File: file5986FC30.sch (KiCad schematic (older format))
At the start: 52 parts, among them Q1 Q_NPN_BEC, Q2 Q_NPN_BEC, Q3 Q_NPN_BEC, Q4 Q_NPN_BEC, U12 CM1224, U15 ufl, U16 ufl, U17 ufl, U3 MIC29302, U5 J502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

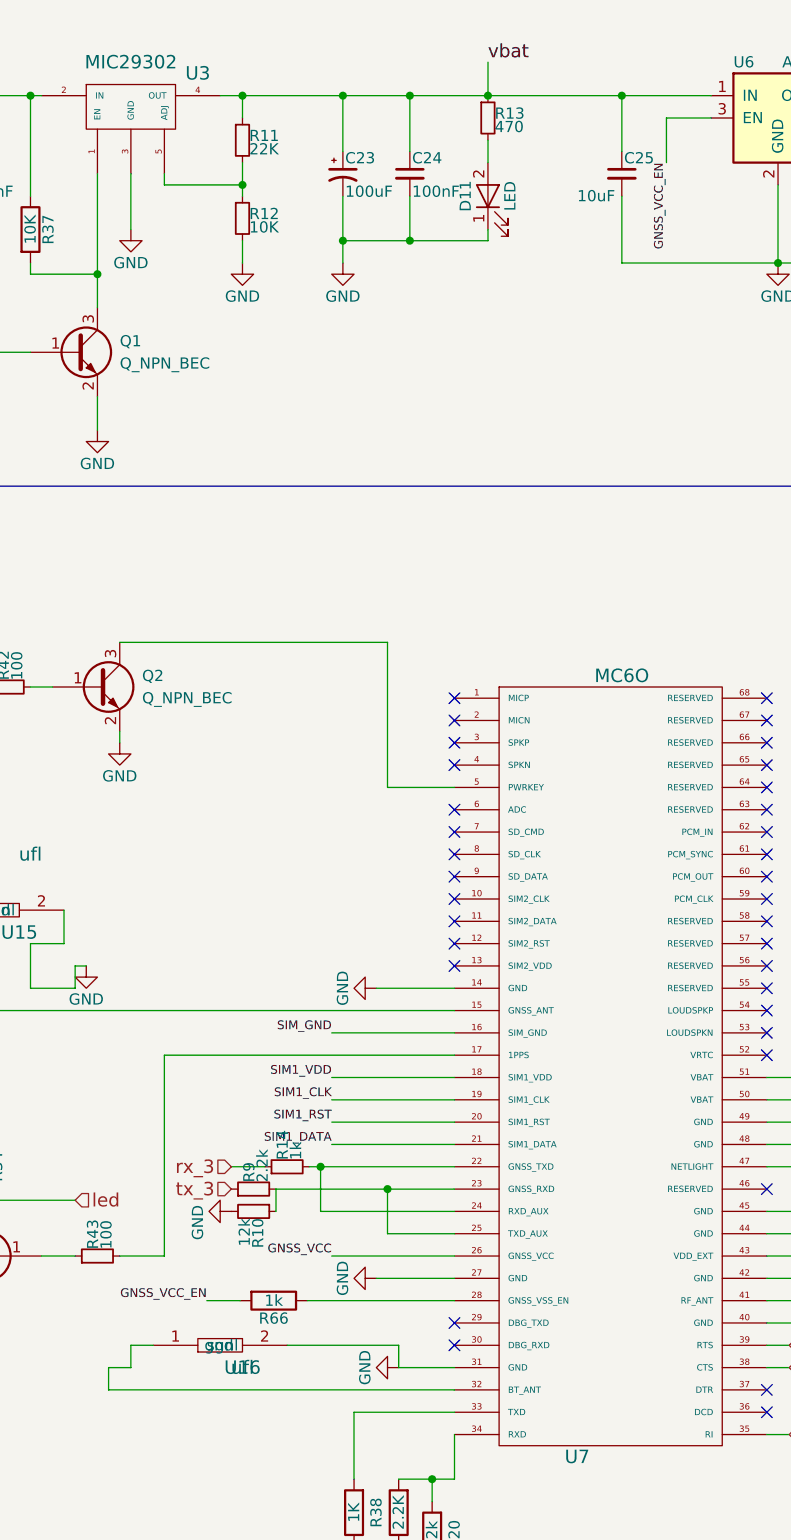
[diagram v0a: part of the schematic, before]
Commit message: Final pcb given to pcbpower
fleet management vim with following features
- ublox m8u, mc60
- mpu6050
- vibration sensor
- buzzer, switches, thottle bypass,
- sim interface according to quectel
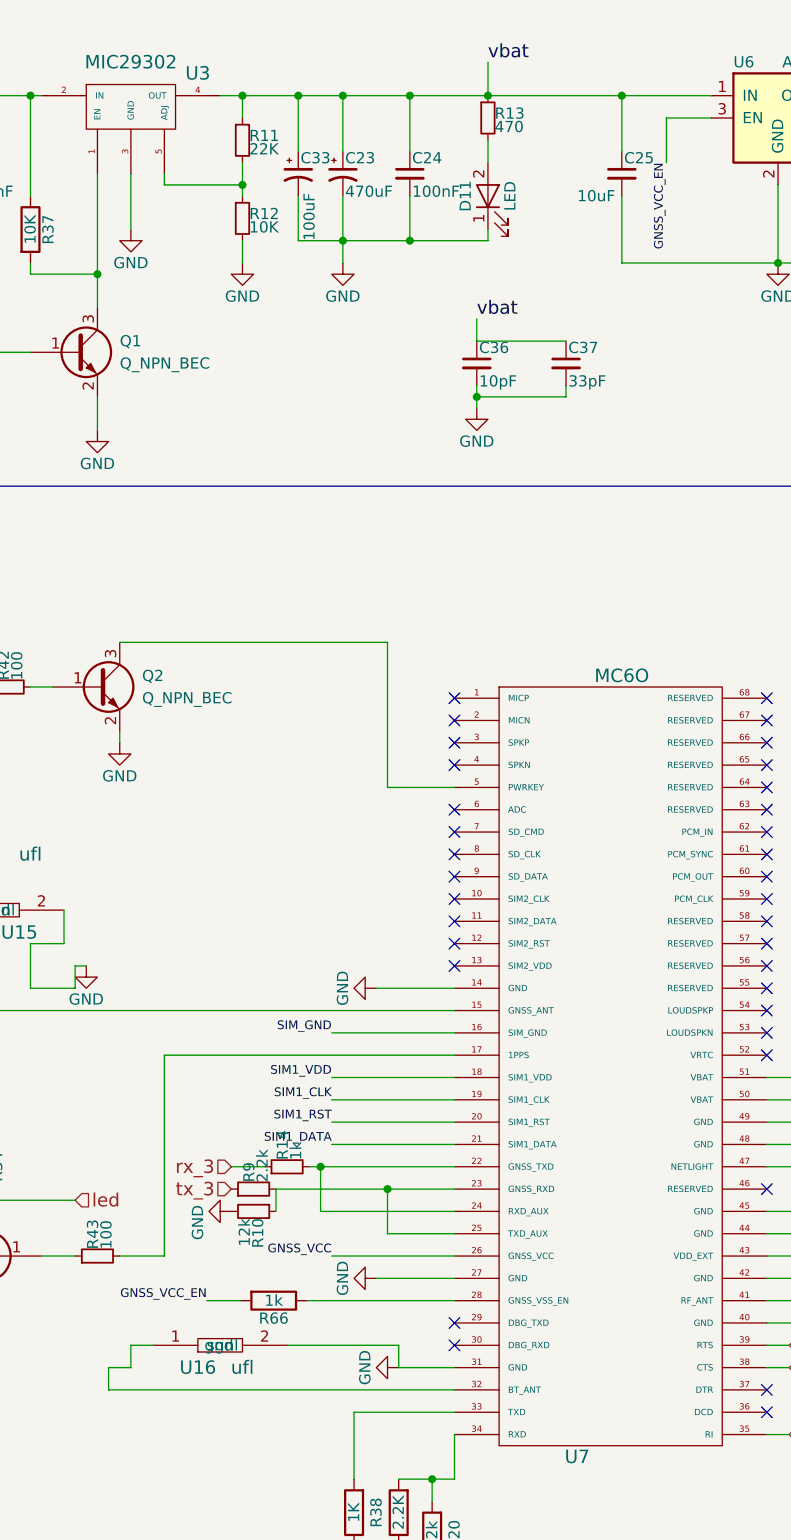
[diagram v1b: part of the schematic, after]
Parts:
- added C33: 100uF, Capacitors_Tantalum_SMD:CP_Tantalum_Case-B_EIA-3528-21_Reflow, symbol CP1_Small
- added C36: 10pF, Capacitors_SMD:C_0603_HandSoldering, symbol C_Small
- added C37: 33pF, Capacitors_SMD:C_0603_HandSoldering, symbol C_Small
- C23: value 100uF -> 470uF
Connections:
- net GND: now also C33.2, C36.2, C37.2
- net vbat: now also C33.1, C36.1, C37.1
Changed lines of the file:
@@
 LIBS:mpu
 LIBS:68 PIN
+LIBS:reugulators
 LIBS:simcard
 LIBS:j502
@@
 P 3300 1100
 F 0 "C23" H 3310 1170 50  0000 L CNN
-F 1 "100uF" H 3310 1020 50  0000 L CNN
+F 1 "470uF" H 3310 1020 50  0000 L CNN
 F 2 "Capacitors_THT:CP_Radial_D5.0mm_P2.50mm" H 3300 1100 50  0001 C CNN
 F 3 "" H 3300 1100 50  0000 C CNN
@@
 U 1 1 5ACB7744
 P 2850 6450
-F 0 "U16" H 2850 6450 60  0000 C CNN
+F 0 "U16" H 2650 6450 60  0000 C CNN
 F 1 "ufl" H 2850 6450 60  0000 C CNN
 F 2 "ufl:ufl_shield" H 2850 6450 60  0001 C CNN
@@
 Connection ~ 3600 750
 Wire Wire Line
-	3300 1400 3950 1400
+	3100 1400 3950 1400
 Wire Wire Line
 	3950 750  3950 600
@@
 Wire Wire Line
 	10400 600  9250 600
+$Comp
+L CP1_Small C33
+U 1 1 5B1E2F2F
+P 3100 1100
+F 0 "C33" H 3110 1170 50  0000 L CNN
+F 1 "100uF" V 3150 800 50  0000 L CNN
+F 2 "Capacitors_Tantalum_SMD:CP_Tantalum_Case-B_EIA-3528-21_Reflow" H 3100 1100 50  0001 C CNN
+F 3 "" H 3100 1100 50  0000 C CNN
+	1    3100 1100
+	1    0    0    -1
+$EndComp
+Wire Wire Line
+	3100 1200 3100 1400
+Wire Wire Line
+	3100 1000 3100 750
+Connection ~ 3100 750
+Text Label 3900 1750 0    60   ~ 0
+vbat
+$Comp
+L C_Small C36
+U 1 1 5B1E5113
+P 3900 1950
+F 0 "C36" H 3910 2020 50  0000 L CNN
+F 1 "10pF" H 3910 1870 50  0000 L CNN
+F 2 "Capacitors_SMD:C_0603_HandSoldering" H 3900 1950 50  0001 C CNN
+F 3 "" H 3900 1950 50  0000 C CNN
+	1    3900 1950
+	1    0    0    -1
+$EndComp
+$Comp
+L C_Small C37
+U 1 1 5B1E51CF
+P 4300 1950
+F 0 "C37" H 4310 2020 50  0000 L CNN
+F 1 "33pF" H 4310 1870 50  0000 L CNN
+F 2 "Capacitors_SMD:C_0603_HandSoldering" H 4300 1950 50  0001 C CNN
+F 3 "" H 4300 1950 50  0000 C CNN
+	1    4300 1950
+	1    0    0    -1
+$EndComp
+Wire Wire Line
+	3900 1750 3900 1850
+Wire Wire Line
+	3900 1850 4300 1850
+Wire Wire Line
+	4300 2050 4300 2100
+Wire Wire Line
+	4300 2100 3900 2100
+Wire Wire Line
+	3900 2050 3900 2150
+$Comp
+L GND #PWR039
+U 1 1 5B1E55C6
+P 3900 2150
+F 0 "#PWR039" H 3900 1900 50  0001 C CNN
+F 1 "GND" H 3900 2000 50  0000 C CNN
+F 2 "" H 3900 2150 50  0000 C CNN
+F 3 "" H 3900 2150 50  0000 C CNN
+	1    3900 2150
+	1    0    0    -1
+$EndComp
+Connection ~ 3900 2100
 $EndSCHEMATC
